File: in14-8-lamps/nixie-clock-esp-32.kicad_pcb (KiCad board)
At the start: 2 copper layers, 153 x 50 mm, 87 parts, among them J1 Conn_01x02_Pin, J2 Conn_01x02_Pin, J3 Conn_01x06_Pin, Q1 MMBTA42, Q10 2N7002, Q11 MMBTA42, Q12 MMBTA92, Q13 MMBTA42, Q14 MMBTA92, Q15 MMBTA42, Q2 MMBTA92, Q3 MMBTA42, Q4 MMBTA92, Q5 MMBTA42, Q6 MMBTA92, Q7 MMBTA42, Q8 MMBTA92, Q9 MMBTA42, U1 max688 boost regulator 5 to 1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, U2 AMS1117-3.3, U3 ESP32-WROOM-32D, U4 DS3231M, U5 74141

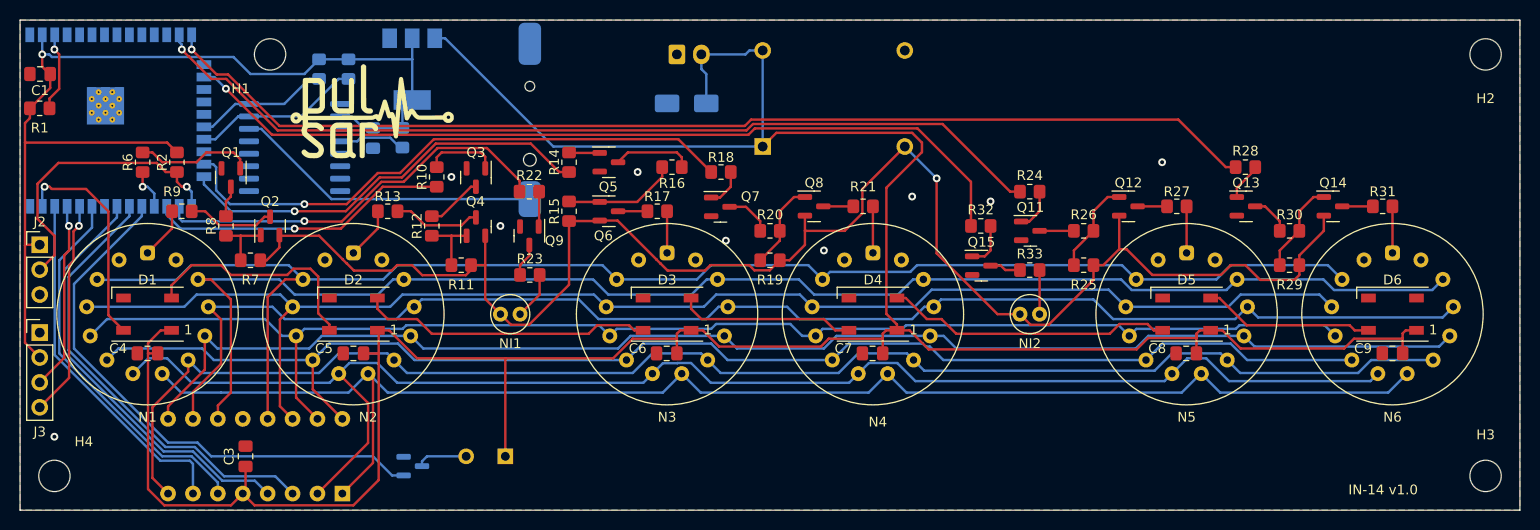
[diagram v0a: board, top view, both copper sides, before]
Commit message: add button and ws2812 connector
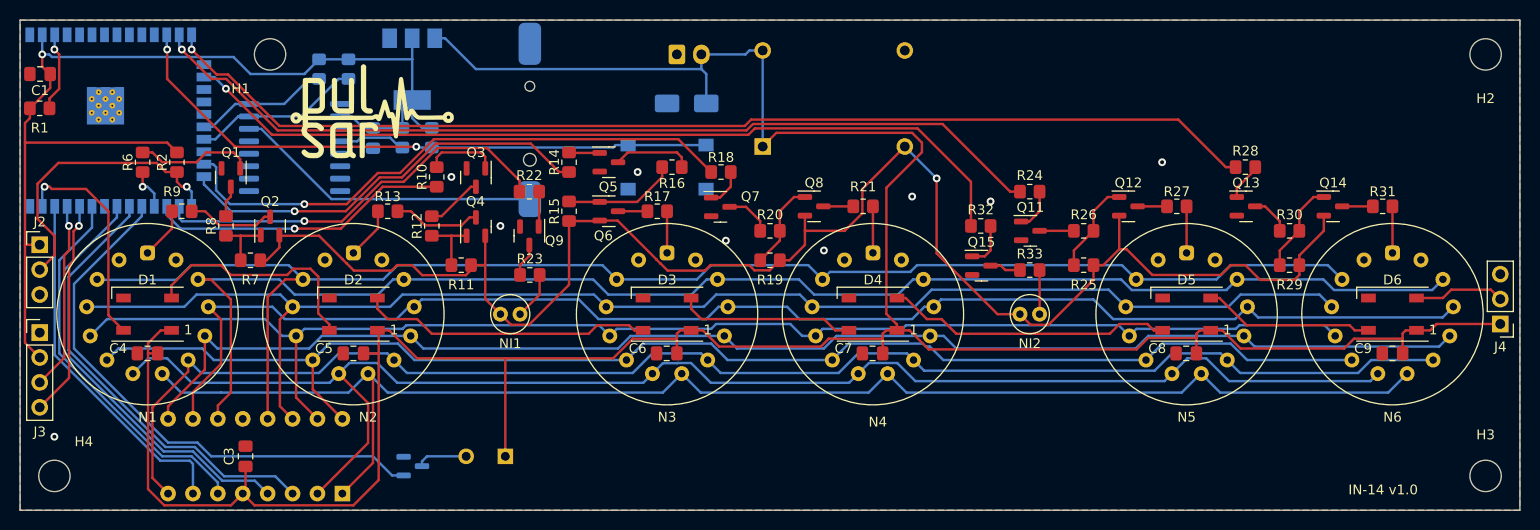
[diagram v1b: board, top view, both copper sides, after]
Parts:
- added J4: Conn_01x02_Pin, Connector_PinHeader_2.54mm:PinHeader_1x03_P2.54mm_Vertical, F.Cu at (201.0, 81.0)
- added R34: 10k, Resistor_SMD:R_0805_2012Metric_Pad1.20x1.40mm_HandSolder, B.Cu at (92.0, 62.0)
- added SW1: SW_Push, Button_Switch_SMD:SW_Push_1P1T_NO_6x6mm_H9.5mm, B.Cu at (116.0, 65.0)
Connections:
- D6 pad 2: unconnected-(D6-DOUT-Pad2) -> /tubes/WS2812_OUT
- U3 pad 12: unconnected-(U3-IO27-Pad12) -> /control/BTN2
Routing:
- net /control/BTN2: track 0.00 -> 62.5 mm, vias 0 -> 2
- net /tubes/WS2812_OUT: track 0.00 -> 9.30 mm
- net +3.3V: track 108.0 -> 112.3 mm
- net +5V: track 293.2 -> 292.5 mm
